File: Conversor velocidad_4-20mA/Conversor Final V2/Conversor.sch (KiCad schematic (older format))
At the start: 1 part, among them K1 DIPxx-1Cxx-51x

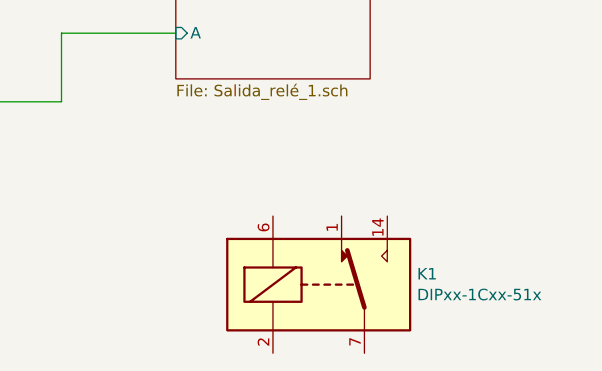
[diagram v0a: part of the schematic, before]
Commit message: Actualizacion Esquematico en bloques
Agregue un par de footprints y acomodé el relé en el bloque correspondiente. Hay que consultar sobre los footprint del 4040 y 4070
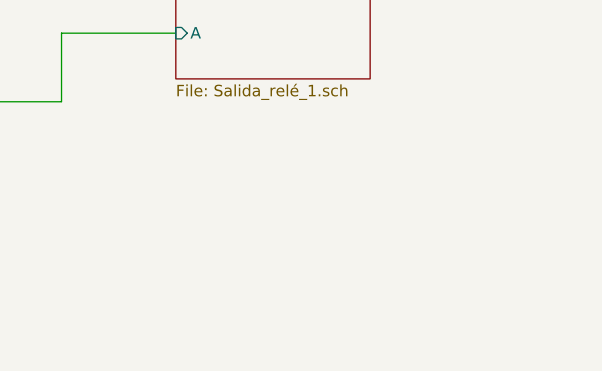
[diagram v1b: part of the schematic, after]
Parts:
- removed K1: DIPxx-1Cxx-51x, Relay_THT:Relay_StandexMeder_DIP_LowProfile, symbol Relay:DIPxx-1Cxx-51x
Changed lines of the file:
@@
 Wire Wire Line
 	3550 2000 2950 2000
-$Comp
-L Relay:DIPxx-1Cxx-51x K1
-U 1 1 612F3E2A
-P 4525 3750
-F 0 "K1" H 4955 3796 50  0000 L CNN
-F 1 "DIPxx-1Cxx-51x" H 4955 3705 50  0000 L CNN
-F 2 "Relay_THT:Relay_StandexMeder_DIP_LowProfile" H 4975 3700 50  0001 L CNN
-F 3 "https://standexelectronics.com/wp-content/uploads/datasheet_reed_relay_DIP.pdf" H 4525 3750 50  0001 C CNN
-	1    4525 3750
-	1    0    0    -1
-$EndComp
 $EndSCHEMATC

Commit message: Agregue footprints
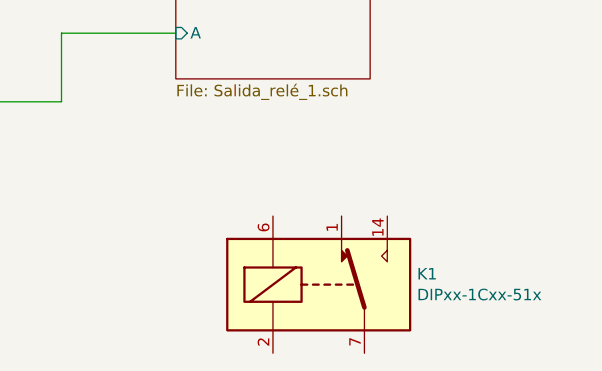
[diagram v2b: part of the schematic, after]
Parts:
- added K1: DIPxx-1Cxx-51x, Relay_THT:Relay_StandexMeder_DIP_LowProfile, symbol Relay:DIPxx-1Cxx-51x
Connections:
- new net: K1.7, K1.8
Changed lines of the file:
@@
 Wire Wire Line
 	3550 2000 2950 2000
+$Comp
+L Relay:DIPxx-1Cxx-51x K1
+U 1 1 612F3E2A
+P 4525 3750
+F 0 "K1" H 4955 3796 50  0000 L CNN
+F 1 "DIPxx-1Cxx-51x" H 4955 3705 50  0000 L CNN
+F 2 "Relay_THT:Relay_StandexMeder_DIP_LowProfile" H 4975 3700 50  0001 L CNN
+F 3 "https://standexelectronics.com/wp-content/uploads/datasheet_reed_relay_DIP.pdf" H 4525 3750 50  0001 C CNN
+	1    4525 3750
+	1    0    0    -1
+$EndComp
 $EndSCHEMATC
